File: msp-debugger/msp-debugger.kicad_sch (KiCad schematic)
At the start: 21 parts, among them J1 USB_B_Micro, J2 Conn_02x10, SW1 SW_MEC_5E, SW2 SW_MEC_5E, SW3 SW_MEC_5E, SW4 SW_MEC_5E, SW5 SW_MEC_5E, SW6 SW_MEC_5E, U1 ESP32-S2-SOLO, U2 NHD-0420H1Z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

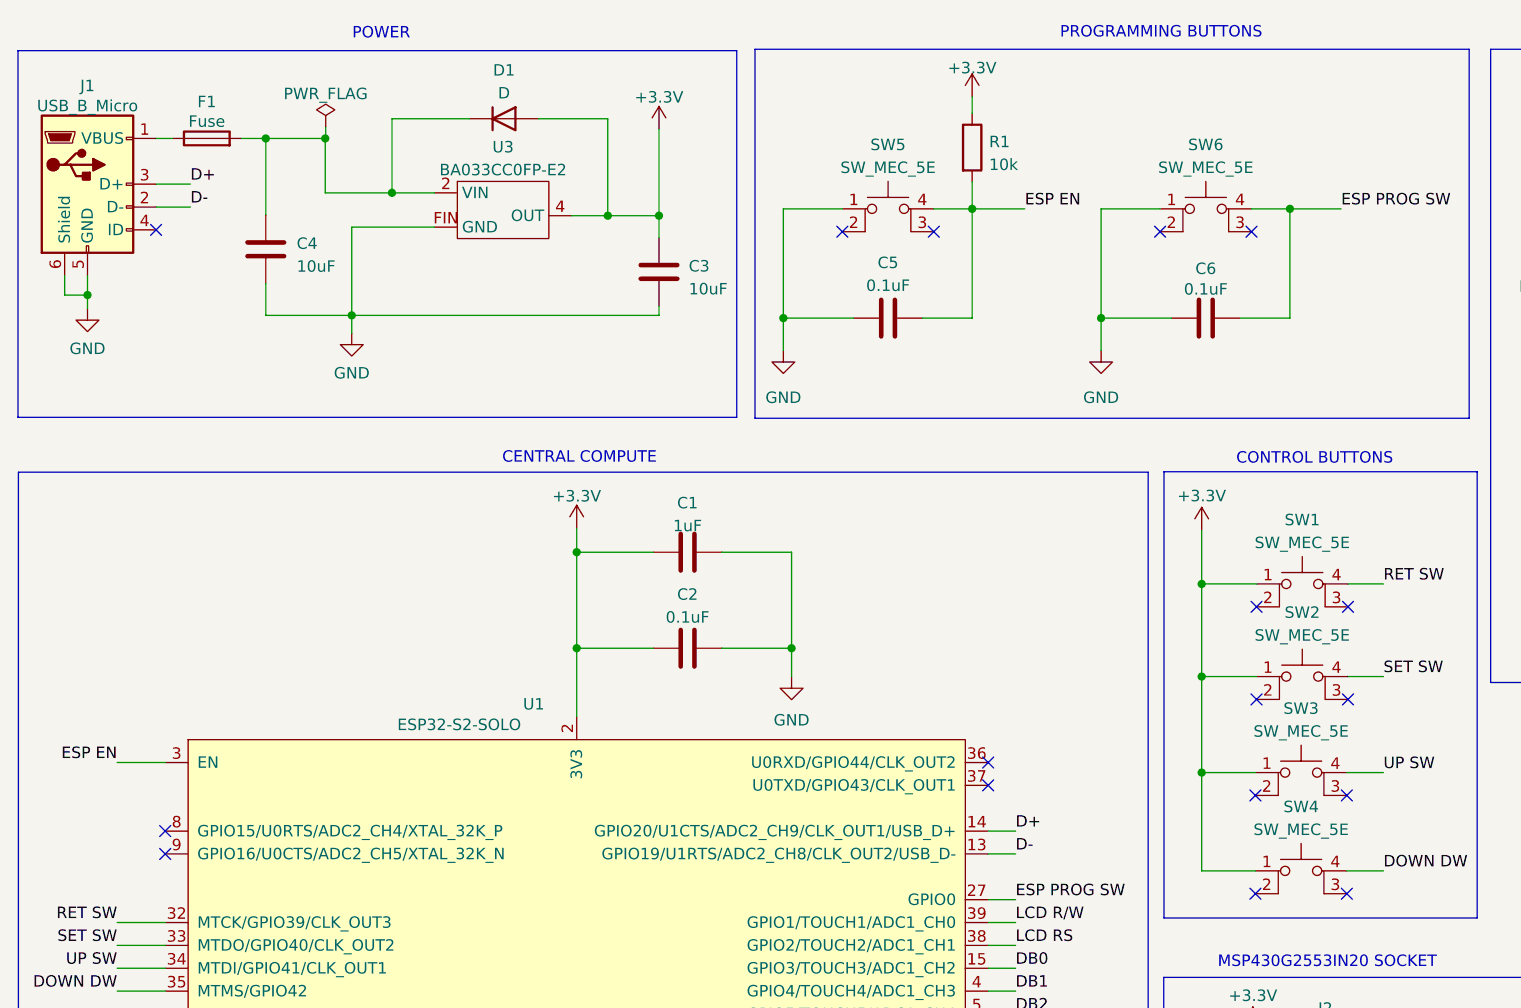
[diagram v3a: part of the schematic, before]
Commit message: complete rough footprints
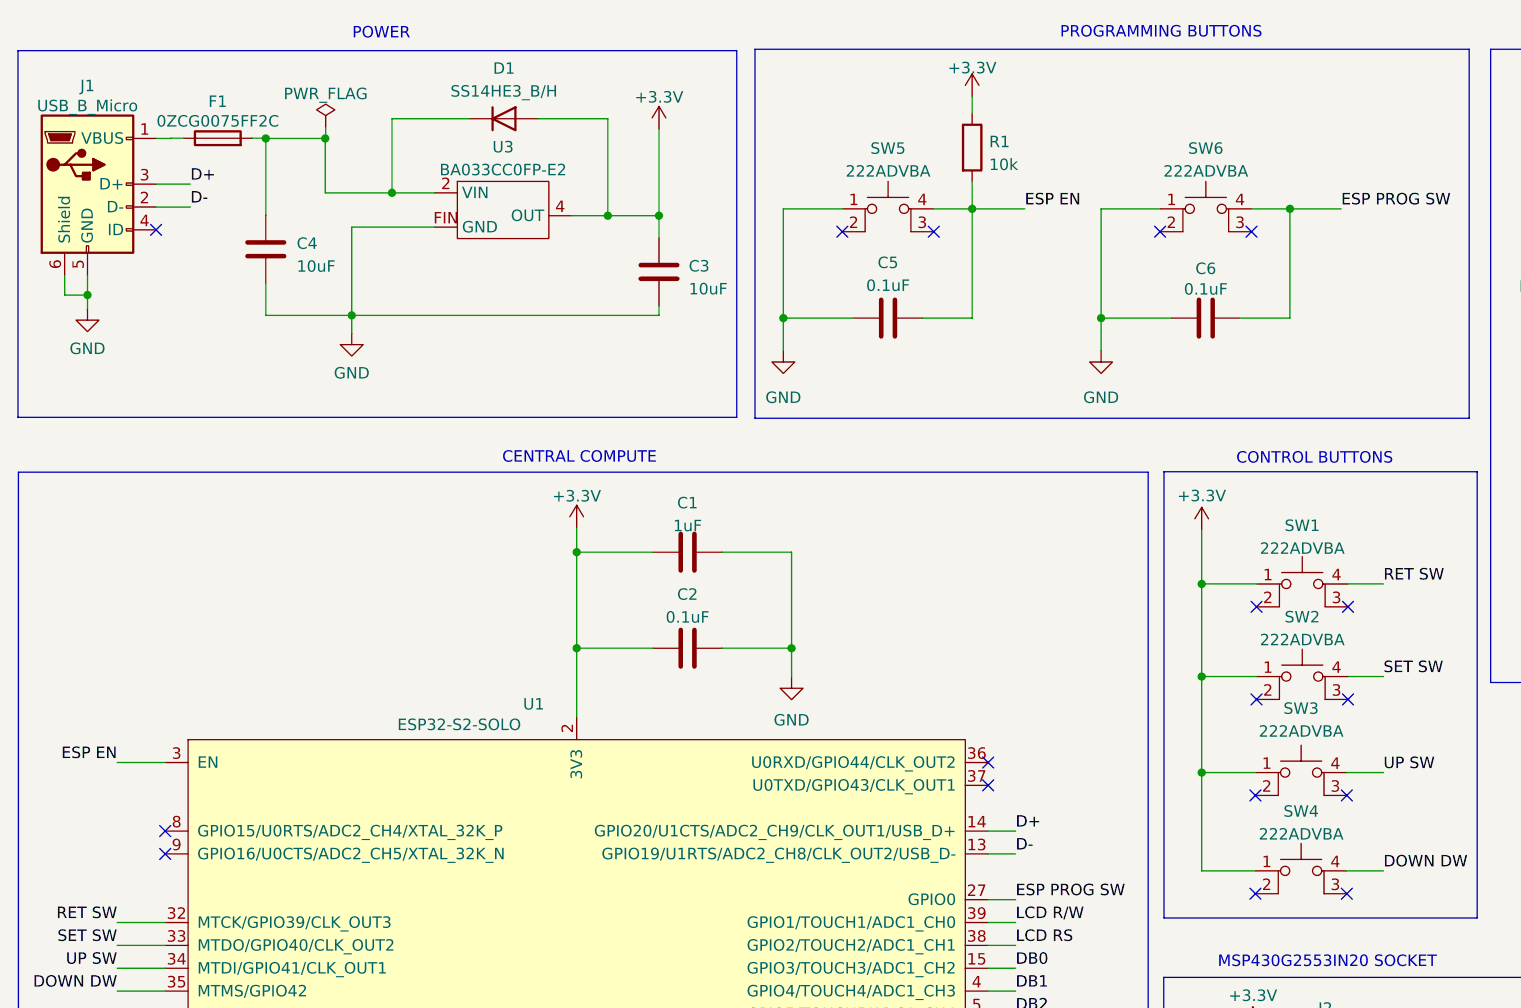
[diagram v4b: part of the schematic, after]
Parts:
- D1: value D -> SS14HE3_B/H
- F1: value Fuse -> 0ZCG0075FF2C
- J2: footprint (none) -> project:DIL_CONN_110-83-320-41-001101
- RV1: footprint (none) -> project:Potentiometer_CTS_PTN10-E20HB20
- SW1, SW2, SW3, SW4, SW5, SW6: value SW_MEC_5E -> 222ADVBA; footprint (none) -> buttons:SW_222ADVBA
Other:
- moved on the sheet: F1
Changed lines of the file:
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@@
     (stroke (width 0) (type default))
   )
-  (wire (pts (xy 55.88 30.6324) (xy 57.7088 30.6324))
+  (wire (pts (xy 57.531 30.607) (xy 58.928 30.607))
     (stroke (width 0) (type default))
   )
@@
     (stroke (width 0) (type default))
   )
+  (wire (pts (xy 57.531 30.6324) (xy 55.88 30.6324))
+    (stroke (width 0) (type default))
+  )
   (wire (pts (xy 77.6224 50.292) (xy 77.6224 52.2732))
     (stroke (width 0) (type default))
@@
     (stroke (width 0) (type default))
   )
-  (wire (pts (xy 65.3288 30.6324) (xy 68.072 30.6324))
+  (wire (pts (xy 66.548 30.607) (xy 68.072 30.607))
+    (stroke (width 0) (type default))
+  )
+  (wire (pts (xy 68.072 30.607) (xy 68.072 30.6324))
     (stroke (width 0) (type default))
   )
@@
     (stroke (width 0) (type default))
   )
+  (wire (pts (xy 57.531 30.607) (xy 57.531 30.6324))
+    (stroke (width 0) (type default))
+  )
   (wire (pts (xy 148.336 148.2344) (xy 151.384 148.2344))
     (stroke (width 0) (type default))
@@
   (symbol (lib_id "Device:D") (at 94.5388 28.448 0) (unit 1)
     (in_bom yes) (on_board yes) (dnp no) (fields_autoplaced)
-    (property "Reference" "D1" (at 94.5388 23.0632 0)
-      (effects (font (size 1.27 1.27)))
-    )
-    (property "Value" "D" (at 94.5388 25.6032 0)
+    (property "Reference" "D1" (at 94.5388 22.86 0)
+      (effects (font (size 1.27 1.27)))
+    )
+    (property "Value" "SS14HE3_B/H" (at 94.5388 25.4 0)
       (effects (font (size 1.27 1.27)))
     )
@@
   (symbol (lib_id "Switch:SW_MEC_5E") (at 172.5168 40.9956 0) (unit 1)
     (in_bom yes) (on_board yes) (dnp no) (fields_autoplaced)
-    (property "Reference" "SW6" (at 172.5168 31.3436 0)
-      (effects (font (size 1.27 1.27)))
-    )
-    (property "Value" "SW_MEC_5E" (at 172.5168 33.8836 0)
-      (effects (font (size 1.27 1.27)))
-    )
-    (property "Footprint" "" (at 172.5168 33.3756 0)
+    (property "Reference" "SW6" (at 172.5168 31.75 0)
+      (effects (font (size 1.27 1.27)))
+    )
+    (property "Value" "222ADVBA" (at 172.5168 34.29 0)
+      (effects (font (size 1.27 1.27)))
+    )
+    (property "Footprint" "buttons:SW_222ADVBA" (at 172.5168 33.3756 0)
       (effects (font (size 1.27 1.27)) hide)
     )
@@
   (symbol (lib_id "Switch:SW_MEC_5E") (at 137.2108 40.9956 0) (unit 1)
     (in_bom yes) (on_board yes) (dnp no) (fields_autoplaced)
-    (property "Reference" "SW5" (at 137.2108 31.3436 0)
-      (effects (font (size 1.27 1.27)))
-    )
-    (property "Value" "SW_MEC_5E" (at 137.2108 33.8836 0)
-      (effects (font (size 1.27 1.27)))
-    )
-    (property "Footprint" "" (at 137.2108 33.3756 0)
+    (property "Reference" "SW5" (at 137.2108 31.75 0)
+      (effects (font (size 1.27 1.27)))
+    )
+    (property "Value" "222ADVBA" (at 137.2108 34.29 0)
+      (effects (font (size 1.27 1.27)))
+    )
+    (property "Footprint" "buttons:SW_222ADVBA" (at 137.2108 33.3756 0)
       (effects (font (size 1.27 1.27)) hide)
     )
@@
       (effects (font (size 1.27 1.27)) (justify right))
     )
-    (property "Footprint" "" (at 245.0592 36.2204 0)
+    (property "Footprint" "project:Potentiometer_CTS_PTN10-E20HB20" (at 245.0592 36.2204 0)
       (effects (font (size 1.27 1.27)) hide)
     )
@@
       (effects (font (size 1.27 1.27)))
     )
-    (property "Value" "SW_MEC_5E" (at 183.1086 96.52 0)
-      (effects (font (size 1.27 1.27)))
-    )
-    (property "Footprint" "" (at 183.1086 96.012 0)
+    (property "Value" "222ADVBA" (at 183.1086 96.52 0)
+      (effects (font (size 1.27 1.27)))
+    )
+    (property "Footprint" "buttons:SW_222ADVBA" (at 183.1086 96.012 0)
       (effects (font (size 1.27 1.27)) hide)
     )
@@
   (symbol (lib_id "Switch:SW_MEC_5E") (at 183.2356 82.677 0) (unit 1)
     (in_bom yes) (on_board yes) (dnp no) (fields_autoplaced)
-    (property "Reference" "SW1" (at 183.2356 73.025 0)
-      (effects (font (size 1.27 1.27)))
-    )
-    (property "Value" "SW_MEC_5E" (at 183.2356 75.565 0)
-      (effects (font (size 1.27 1.27)))
-    )
-    (property "Footprint" "" (at 183.2356 75.057 0)
+    (property "Reference" "SW1" (at 183.2356 73.66 0)
+      (effects (font (size 1.27 1.27)))
+    )
+    (property "Value" "222ADVBA" (at 183.2356 76.2 0)
+      (effects (font (size 1.27 1.27)))
+    )
+    (property "Footprint" "buttons:SW_222ADVBA" (at 183.2356 75.057 0)
       (effects (font (size 1.27 1.27)) hide)
     )
@@
     )
   )
-  (symbol (lib_id "Device:Fuse") (at 61.5188 30.6324 90) (unit 1)
+  (symbol (lib_id "Device:Fuse") (at 62.738 30.607 90) (unit 1)
     (in_bom yes) (on_board yes) (dnp no)
-    (property "Reference" "F1" (at 61.5188 26.5684 90)
-      (effects (font (size 1.27 1.27)))
-    )
-    (property "Value" "Fuse" (at 61.5188 28.7528 90)
-      (effects (font (size 1.27 1.27)))
-    )
-    (property "Footprint" "Fuse:Fuse_1812_4532Metric" (at 61.5188 32.4104 90)
-      (effects (font (size 1.27 1.27)) hide)
-    )
-    (property "Datasheet" "~" (at 61.5188 30.6324 0)
+    (property "Reference" "F1" (at 62.738 26.543 90)
+      (effects (font (size 1.27 1.27)))
+    )
+    (property "Value" "0ZCG0075FF2C" (at 62.738 28.7274 90)
+      (effects (font (size 1.27 1.27)))
+    )
+    (property "Footprint" "Fuse:Fuse_1812_4532Metric" (at 62.738 32.385 90)
+      (effects (font (size 1.27 1.27)) hide)
+    )
+    (property "Datasheet" "~" (at 62.738 30.607 0)
       (effects (font (size 1.27 1.27)) hide)
     )
@@
       (effects (font (size 1.27 1.27)))
     )
-    (property "Footprint" "" (at 184.404 143.8148 0)
+    (property "Footprint" "project:DIL_CONN_110-83-320-41-001101" (at 184.404 143.8148 0)
       (effects (font (size 1.27 1.27)) hide)
     )
@@
   (symbol (lib_id "Switch:SW_MEC_5E") (at 183.2356 92.964 0) (unit 1)
     (in_bom yes) (on_board yes) (dnp no) (fields_autoplaced)
-    (property "Reference" "SW2" (at 183.2356 83.312 0)
-      (effects (font (size 1.27 1.27)))
-    )
-    (property "Value" "SW_MEC_5E" (at 183.2356 85.852 0)
-      (effects (font (size 1.27 1.27)))
-    )
-    (property "Footprint" "" (at 183.2356 85.344 0)
+    (property "Reference" "SW2" (at 183.2356 83.82 0)
+      (effects (font (size 1.27 1.27)))
+    )
+    (property "Value" "222ADVBA" (at 183.2356 86.36 0)
+      (effects (font (size 1.27 1.27)))
+    )
+    (property "Footprint" "buttons:SW_222ADVBA" (at 183.2356 85.344 0)
       (effects (font (size 1.27 1.27)) hide)
     )
@@
   (symbol (lib_id "Switch:SW_MEC_5E") (at 183.1086 114.554 0) (unit 1)
     (in_bom yes) (on_board yes) (dnp no) (fields_autoplaced)
-    (property "Reference" "SW4" (at 183.1086 104.902 0)
-      (effects (font (size 1.27 1.27)))
-    )
-    (property "Value" "SW_MEC_5E" (at 183.1086 107.442 0)
-      (effects (font (size 1.27 1.27)))
-    )
-    (property "Footprint" "" (at 183.1086 106.934 0)
-      (effects (font (size 1.27 1.27)) hide)
-    )
+    (property "Reference" "SW4" (at 183.1086 105.41 0)
+      (effects (font (size 1.27 1.27)))
+    )
+    (property "Value" "222ADVBA" (at 183.1086 107.95 0)
+      (effects (font (size 1.27 1.27)))
+    )
+    (property "Footprint" "buttons:SW_222ADVBA" (at 183.1086 106.934 0)
+      (effects (font (size 1.27 1.27)) hide)
+    )

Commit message: route rough traces
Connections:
- net +3.3V: now also U3.3 (OUT); no longer U3.4 (OUT)
- net DB0: now also U1.24 (SPIIO4/GPIO33/FSPIHD); no longer U1.15 (GPIO3/TOUCH3/ADC1_CH2)
- net DB1: now also U1.25 (SPIIO5/GPIO34/FSPICS0); no longer U1.4 (GPIO4/TOUCH4/ADC1_CH3)
- net DB2: now also U1.21 (GPIO13/TOUCH13/ADC2_CH2/FSPIQ/FSPIIO7); no longer U1.5 (GPIO5/TOUCH5/ADC1_CH4)
- net DB3: now also U1.20 (GPIO12/TOUCH12/ADC2_CH1/FSPICLK/FSPIIO6); no longer U1.6 (GPIO6/TOUCH6/ADC1_CH5)
- net DB4: now also U1.19 (GPIO11/TOUCH11/ADC2_CH0/FSPID/FSPIIO5); no longer U1.7 (GPIO7/TOUCH7/ADC1_CH6)
- net DB5: now also U1.18 (GPIO10/TOUCH10/ADC1_CH9/FSPICS0/FSPIIO4); no longer U1.12 (GPIO8/TOUCH8/ADC1_CH7)
- net DB7: now also U1.15 (GPIO3/TOUCH3/ADC1_CH2); no longer U1.18 (GPIO10/TOUCH10/ADC1_CH9/FSPICS0/FSPIIO4)
- net DOWN DW: now also U1.29 (SPIIO7/GPIO36/FSPICLK); no longer U1.35 (MTMS/GPIO42)
- net GND: now also U3.4 (GND); no longer U3.FIN (GND)
- net LCD RS: now also U1.22 (GPIO14/TOUCH14/ADC2_CH3/FSPIWP/FSPIDQS); no longer U1.38 (GPIO2/TOUCH2/ADC1_CH1)
- net LCD R/W: now also U1.23 (GPIO21); no longer U1.39 (GPIO1/TOUCH1/ADC1_CH0)
- net RET SW: now also U1.28 (SPIIO6/GPIO35/FSPID); no longer U1.32 (MTCK/GPIO39/CLK_OUT3)
- net RST: now also U1.8 (GPIO15/U0RTS/ADC2_CH4/XTAL_32K_P); no longer U1.19 (GPIO11/TOUCH11/ADC2_CH0/FSPID/FSPIIO5)
- net SET SW: now also U1.31 (GPIO38/FSPIWP); no longer U1.33 (MTDO/GPIO40/CLK_OUT2)
- net TCK: now also U1.5 (GPIO5/TOUCH5/ADC1_CH4); no longer U1.22 (GPIO14/TOUCH14/ADC2_CH3/FSPIWP/FSPIDQS)
- net TDI: now also U1.6 (GPIO6/TOUCH6/ADC1_CH5); no longer U1.10 (GPIO17/U1TXD/ADC2_CH6/DAC_1)
- net TDO: now also U1.7 (GPIO7/TOUCH7/ADC1_CH6); no longer U1.11 (GPIO18/U1RXD/ADC2_CH7/DAC_2/CLK_OUT3)
- net TEST: now also U1.9 (GPIO16/U0CTS/ADC2_CH5/XTAL_32K_N); no longer U1.20 (GPIO12/TOUCH12/ADC2_CH1/FSPICLK/FSPIIO6)
- net TMS: now also U1.4 (GPIO4/TOUCH4/ADC1_CH3); no longer U1.21 (GPIO13/TOUCH13/ADC2_CH2/FSPIQ/FSPIIO7)
- net UP SW: now also U1.30 (SPIDQS/GPIO37/FSPIQ); no longer U1.34 (MTDI/GPIO41/CLK_OUT1)
- net at C4.1, D1.1 (K), F1.2: now also U3.1 (Vcc); no longer U3.2 (VIN)
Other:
- moved on the sheet: C3, C4, D1, F1, J1, U3

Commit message: rough draft layout
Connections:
- net DB0: now also U1.19 (GPIO11/TOUCH11/ADC2_CH0/FSPID/FSPIIO5); no longer U1.24 (SPIIO4/GPIO33/FSPIHD)
- net DB1: now also U1.20 (GPIO12/TOUCH12/ADC2_CH1/FSPICLK/FSPIIO6); no longer U1.25 (SPIIO5/GPIO34/FSPICS0)
- net DB2: now also U1.12 (GPIO8/TOUCH8/ADC1_CH7); no longer U1.21 (GPIO13/TOUCH13/ADC2_CH2/FSPIQ/FSPIIO7)
- net DB3: now also U1.11 (GPIO18/U1RXD/ADC2_CH7/DAC_2/CLK_OUT3); no longer U1.20 (GPIO12/TOUCH12/ADC2_CH1/FSPICLK/FSPIIO6)
- net DB4: now also U1.10 (GPIO17/U1TXD/ADC2_CH6/DAC_1); no longer U1.19 (GPIO11/TOUCH11/ADC2_CH0/FSPID/FSPIIO5)
- net DB5: now also U1.9 (GPIO16/U0CTS/ADC2_CH5/XTAL_32K_N); no longer U1.18 (GPIO10/TOUCH10/ADC1_CH9/FSPICS0/FSPIIO4)
- net DB6: now also U1.8 (GPIO15/U0RTS/ADC2_CH4/XTAL_32K_P); no longer U1.17 (GPIO9/TOUCH9/ADC1_CH8/FSPIHD)
- net DB7: now also U1.7 (GPIO7/TOUCH7/ADC1_CH6); no longer U1.15 (GPIO3/TOUCH3/ADC1_CH2)
- net LCD RS: now also U1.17 (GPIO9/TOUCH9/ADC1_CH8/FSPIHD); no longer U1.22 (GPIO14/TOUCH14/ADC2_CH3/FSPIWP/FSPIDQS)
- net LCD R/W: now also U1.18 (GPIO10/TOUCH10/ADC1_CH9/FSPICS0/FSPIIO4); no longer U1.23 (GPIO21)
- net RET SW: now also SW2.4 (A); no longer SW1.4 (A)
- net RST: now also U1.22 (GPIO14/TOUCH14/ADC2_CH3/FSPIWP/FSPIDQS); no longer U1.8 (GPIO15/U0RTS/ADC2_CH4/XTAL_32K_P)
- net SET SW: now also SW1.4 (A), U1.29 (SPIIO7/GPIO36/FSPICLK); no longer SW2.4 (A), U1.31 (GPIO38/FSPIWP)
- net TCK: now also U1.25 (SPIIO5/GPIO34/FSPICS0); no longer U1.5 (GPIO5/TOUCH5/ADC1_CH4)
- net TDI: now also U1.24 (SPIIO4/GPIO33/FSPIHD); no longer U1.6 (GPIO6/TOUCH6/ADC1_CH5)
- net TDO: now also U1.23 (GPIO21); no longer U1.7 (GPIO7/TOUCH7/ADC1_CH6)
- net TEST: now also U1.21 (GPIO13/TOUCH13/ADC2_CH2/FSPIQ/FSPIIO7); no longer U1.9 (GPIO16/U0CTS/ADC2_CH5/XTAL_32K_N)
- net TMS: now also U1.26 (GPIO45); no longer U1.4 (GPIO4/TOUCH4/ADC1_CH3)
- net UP SW: now also U1.5 (GPIO5/TOUCH5/ADC1_CH4); no longer U1.30 (SPIDQS/GPIO37/FSPIQ)
- net DOWN DW renamed DOWN SW
- net DOWN SW: now also U1.6 (GPIO6/TOUCH6/ADC1_CH5); no longer U1.29 (SPIIO7/GPIO36/FSPICLK)

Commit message: add test points
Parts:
- added TP1, TP2: TestPoint, TestPoint:TestPoint_Pad_1.5x1.5mm, symbol Connector:TestPoint
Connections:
- net ESP EN: now also TP1.1
- net ESP PROG SW: now also TP2.1
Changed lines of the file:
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@@
 (kicad_sch (version 20230121) (generator eeschema)
   (paper "A4")
+  (junction (at 151.13 115.062) (diameter 0) (color 0 0 0 0)
+  )
   (junction (at 172.0596 101.092) (diameter 0) (color 0 0 0 0)
   )
@@
   )
   (junction (at 181.864 38.4556) (diameter 0) (color 0 0 0 0)
+  )
+  (junction (at 54.864 99.822) (diameter 0) (color 0 0 0 0)
   )
   (junction (at 81.153 38.354) (diameter 0) (color 0 0 0 0)
@@
     (stroke (width 0) (type default))
   )
+  (wire (pts (xy 54.864 99.822) (xy 57.15 99.822))
+    (stroke (width 0) (type default))
+  )
   (wire (pts (xy 132.1308 38.4556) (xy 125.5776 38.4556))
     (stroke (width 0) (type default))
@@
     (stroke (width 0) (type default))
   )
+  (wire (pts (xy 151.13 115.062) (xy 152.4 115.062))
+    (stroke (width 0) (type default))
+  )
   (wire (pts (xy 102.87 73.66) (xy 102.87 76.6064))
     (stroke (width 0) (type default))
@@
     (stroke (width 0) (type default))
   )
-  (wire (pts (xy 148.59 115.062) (xy 151.638 115.062))
+  (wire (pts (xy 148.59 115.062) (xy 151.13 115.062))
     (stroke (width 0) (type default))
   )
@@
     (stroke (width 0) (type default))
   )
+  (wire (pts (xy 151.13 115.062) (xy 151.13 117.094))
+    (stroke (width 0) (type default))
+  )
   (wire (pts (xy 214.9348 71.0184) (xy 220.1672 71.0184))
     (stroke (width 0) (type default))
@@
     (stroke (width 0) (type default))
   )
-  (wire (pts (xy 51.816 99.822) (xy 57.15 99.822))
+  (wire (pts (xy 51.816 99.822) (xy 54.864 99.822))
     (stroke (width 0) (type default))
   )
@@
   )
   (wire (pts (xy 106.0704 30.226) (xy 106.0704 39.624))
+    (stroke (width 0) (type default))
+  )
+  (wire (pts (xy 54.864 95.25) (xy 54.864 99.822))
     (stroke (width 0) (type default))
   )
@@
     (effects (font (size 1.27 1.27)) (justify left bottom))
   )
-  (label "ESP PROG SW" (at 151.638 115.062 0) (fields_autoplaced)
+  (label "ESP PROG SW" (at 152.4 115.062 0) (fields_autoplaced)
     (effects (font (size 1.27 1.27)) (justify left bottom))
   )
@@
         (path "/045ba461-bcb4-4373-9dc5-687bfd2826ef"
           (reference "C5") (unit 1)
+        )
+      )
+    )
+  )
+  (symbol (lib_id "Connector:TestPoint") (at 54.864 95.25 0) (unit 1)
+    (in_bom yes) (on_board yes) (dnp no) (fields_autoplaced)
+    (property "Reference" "TP1" (at 57.15 91.313 0)
+      (effects (font (size 1.27 1.27)) (justify left))
+    )
+    (property "Value" "TestPoint" (at 57.15 93.853 0)
+      (effects (font (size 1.27 1.27)) (justify left))
+    )
+    (property "Footprint" "TestPoint:TestPoint_Pad_1.5x1.5mm" (at 59.944 95.25 0)
+      (effects (font (size 1.27 1.27)) hide)
+    )
+    (property "Datasheet" "~" (at 59.944 95.25 0)
+      (effects (font (size 1.27 1.27)) hide)
+    )
+    (pin "1")
+    (instances
+      (project "msp-debugger"
+        (path "/045ba461-bcb4-4373-9dc5-687bfd2826ef"
+          (reference "TP1") (unit 1)
         )
       )
@@
         )
       )
+    )
+  )
+  (symbol (lib_id "Connector:TestPoint") (at 151.13 117.094 180) (unit 1)
+    (in_bom yes) (on_board yes) (dnp no) (fields_autoplaced)
+    (property "Reference" "TP2" (at 153.162 119.761 0)
+      (effects (font (size 1.27 1.27)) (justify right))
+    )
+    (property "Value" "TestPoint" (at 153.162 122.301 0)
+      (effects (font (size 1.27 1.27)) (justify right))
+    )
+    (property "Footprint" "TestPoint:TestPoint_Pad_1.5x1.5mm" (at 146.05 117.094 0)
+      (effects (font (size 1.27 1.27)) hide)
+    )
+    (property "Datasheet" "~" (at 146.05 117.094 0)
+      (effects (font (size 1.27 1.27)) hide)
+    )
+    (pin "1")
+    (instances
+      (project "msp-debugger"
+        (path "/045ba461-bcb4-4373-9dc5-687bfd2826ef"
+          (reference "TP2") (unit 1)
+        )
+      )
